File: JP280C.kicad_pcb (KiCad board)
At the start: 2 copper layers, 160 x 100 mm, 25 parts, among them J1 Ribbon Cable (A), J2 Ribbon Cable (B), J3 Ribbon Cable (C), J4 Meters

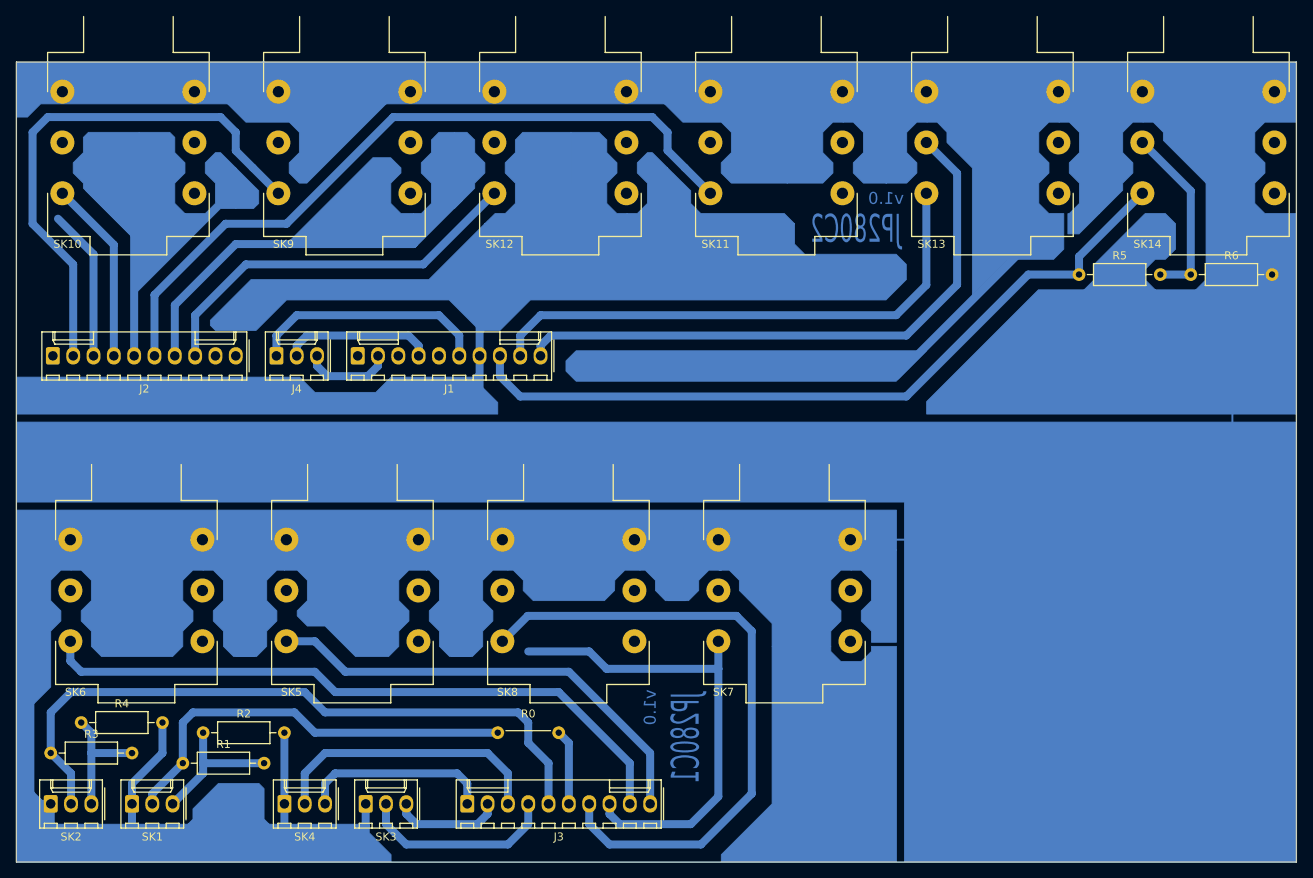
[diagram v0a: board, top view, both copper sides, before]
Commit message: narrowed JP208C1 to 107 mm; added engravings to Cmts.User layer
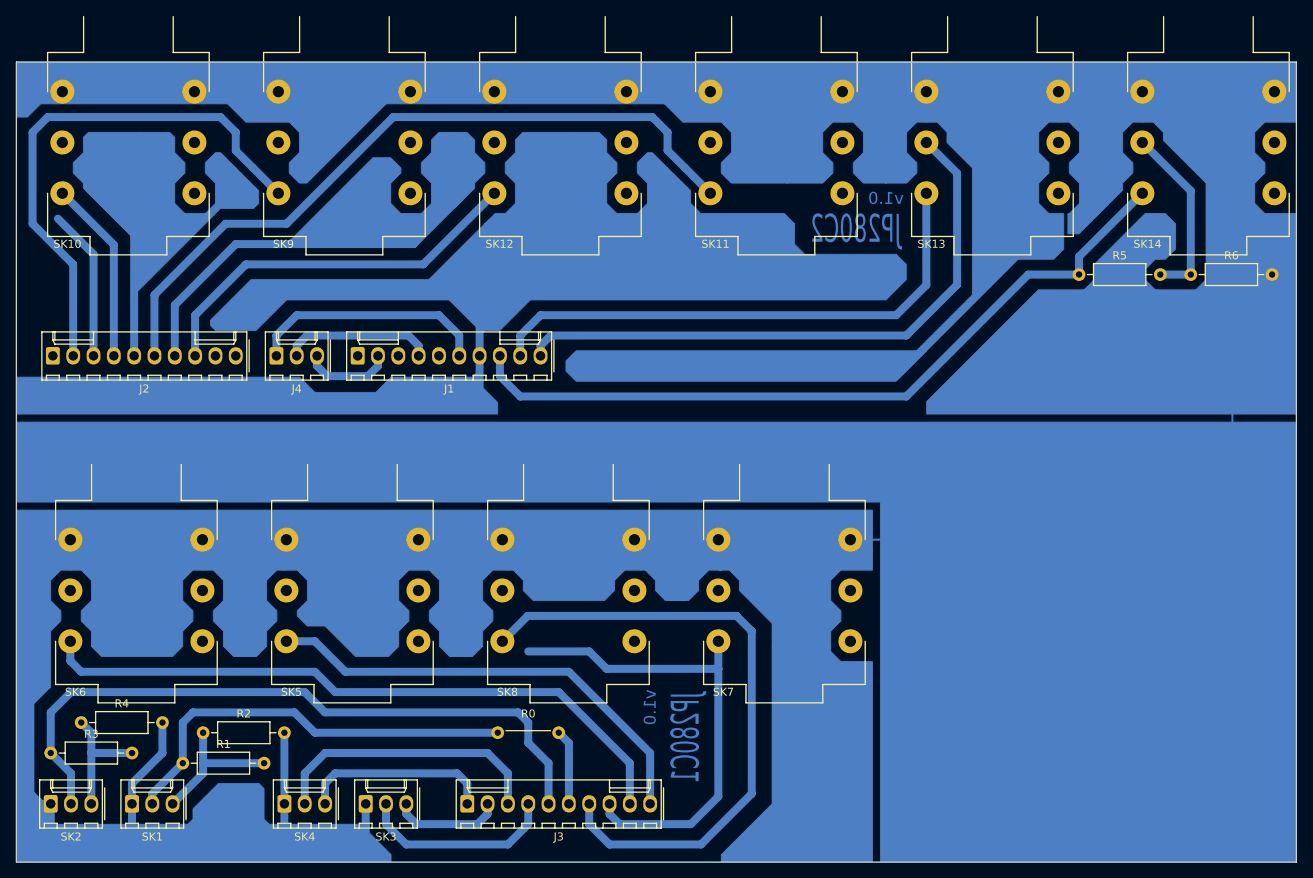
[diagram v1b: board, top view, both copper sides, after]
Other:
- board text added: "(A)"
- board text added: "(B)"
- board text added: "(C)"
- board text added: "L"
- board text added: "L Bus"
- board text added: "L Insert"
- board text added: "Meters"
- board text added: "PFL"
- board text added: "R"
- board text added: "R Bus"
- board text added: "R Insert"
- board text added: "R1"
- board text added: "R2"
- board text added: "R3"
- board text added: "R4"
- board text added: "R5"
- board text added: "R6"
- board text added: "SK10"
- board text added: "SK11"
- board text added: "SK12"
- board text added: "SK13"
- board text added: "SK14"
- board text added: "SK5"
- board text added: "SK6"
- board text added: "SK7"
- board text added: "SK8"
- board text added: "SK9"
